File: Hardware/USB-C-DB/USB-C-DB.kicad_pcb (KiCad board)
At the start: 4 copper layers, 85.6 x 54 mm, 215 parts, among them J1 USB_C_Receptacle, J10 GND, J11 MCU_RST, J12 MCU_EN, J13 MCU_TOUT, J14 MCU_IO0, J15 EFUSE_PRG, J16 UART_DTRN, J17 UART_RTSN, J18 NOT_SUSP, J19 IBUS_S+, J2 EFPROG_POS, J20 IBUS_S-, J21 RESETN, J22 DEBUGGER, J23 +5V, J24 PWM_BC, J25 GND, J3 EFPROG_NEG, J4 BatTP+, J6 BatTP-, J7 P3V3, J8 VBUS, J9 FT_VCCIO, Q1 XP262N7002TR-G, Q10 XP262N7002TR-G, Q2 XP262N7002TR-G, Q3 XP262N7002TR-G, Q4 XP262N7002TR-G, Q5 XP262N7002TR-G, Q6 XP262N7002TR-G, Q7 XP262N7002TR-G, Q8 XP262N7002TR-G, Q9 XP262N7002TR-G, U1 NUF2221W1T2G, U10 NA555D, U2 LD1117S33TR_SOT223, U3 FT260S-U, U4 ESP-WROOM-02, U5 74HC595_mod, U6 74HC595, U7 74HC595, U8 74HC595, U9 74HC595

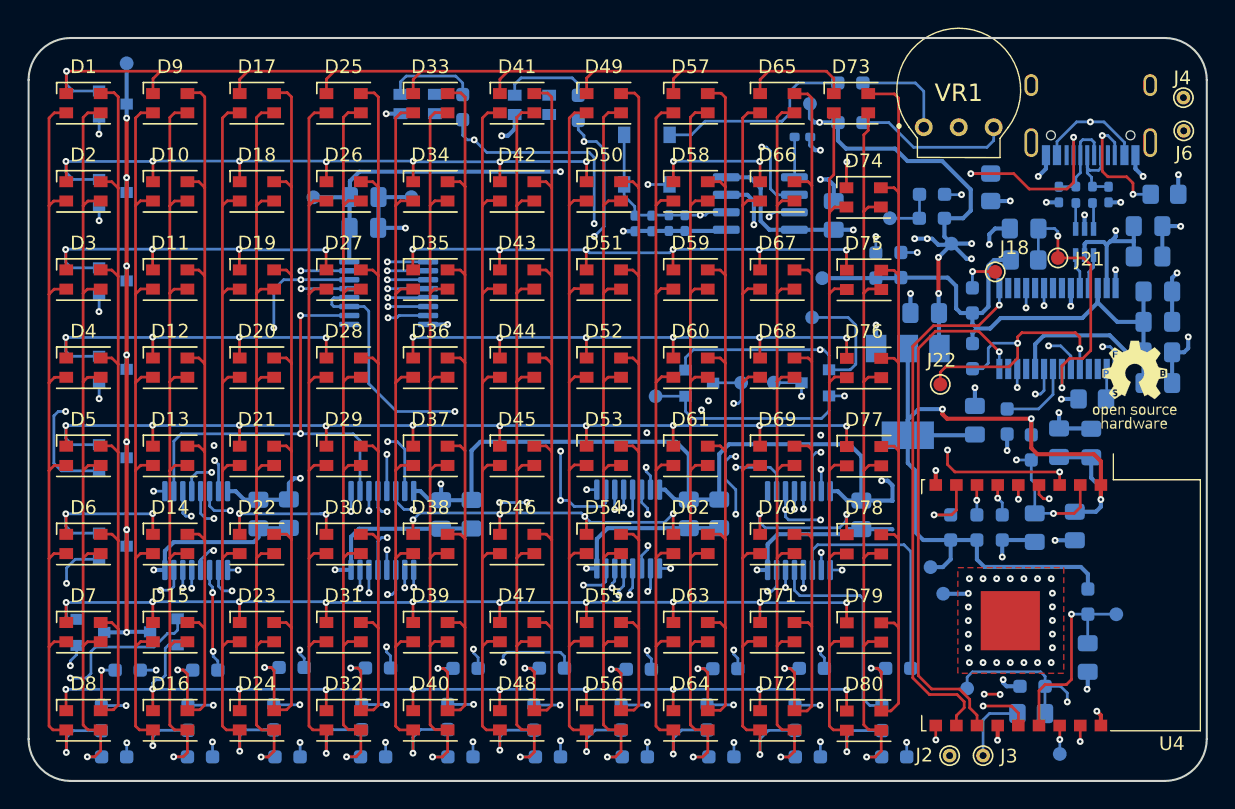
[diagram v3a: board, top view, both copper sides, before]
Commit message: Updating schematic to replace FT260 for FT231
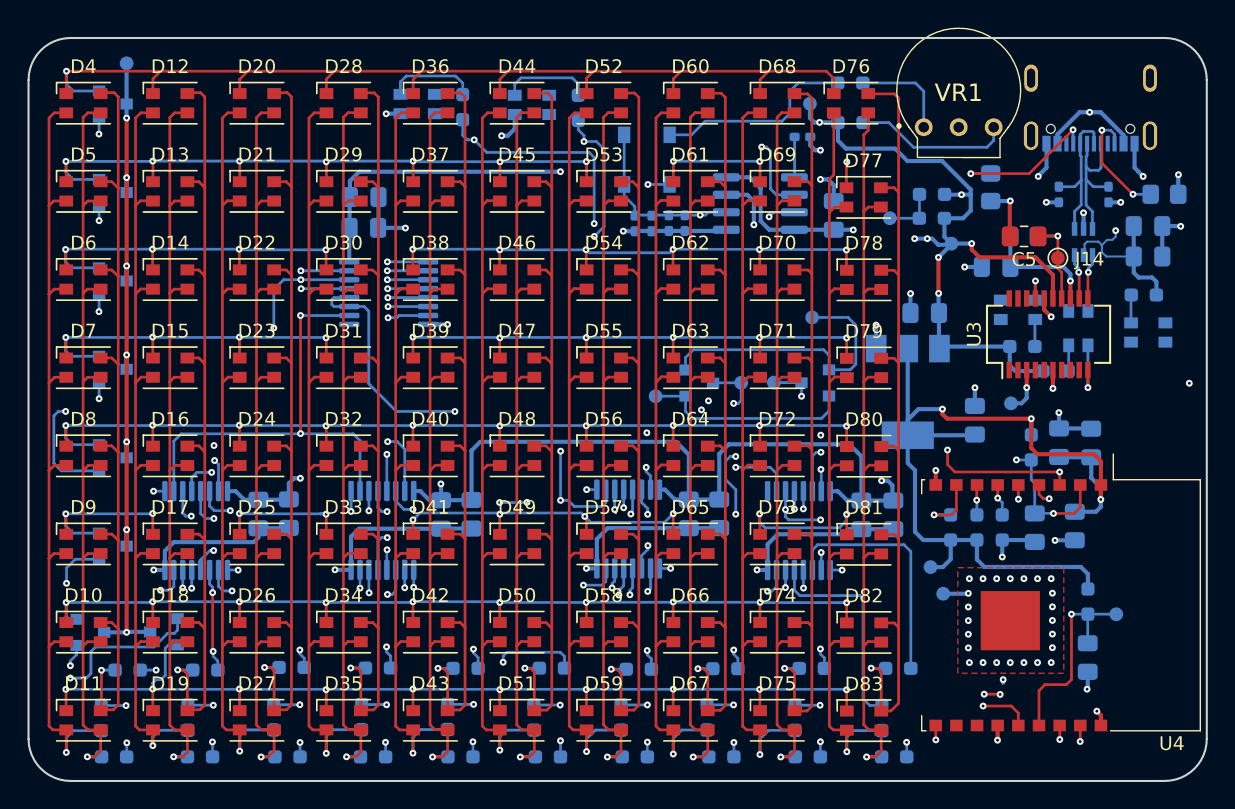
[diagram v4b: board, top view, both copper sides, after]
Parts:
- removed the C10 at (250.4, 124.4)
- removed the C2 at (240.7, 115.4)
- removed the C7 at (250.4, 122.2)
- removed the C9 at (250.4, 120.0)
- removed the J13 at (243.3, 153.6)
- removed J15: EFUSE_PRG, TestPoint:TestPoint_Pad_D1.0mm
- removed J18: NOT_SUSP, TestPoint:TestPoint_Pad_D1.0mm
- removed the J2 at (235.3, 153.7)
- removed J21: RESETN, TestPoint:TestPoint_Pad_D1.0mm
- removed J22: DEBUGGER, TestPoint:TestPoint_Pad_D1.0mm
- removed J23: +5V, TestPoint:TestPoint_Pad_D1.0mm
- removed J25: GND, TestPoint:TestPoint_Pad_D1.0mm
- removed the J3 at (237.7, 153.7)
- removed the J4 at (252.3, 105.9)
- removed the J6 at (252.3, 108.3)
- removed the R10 at (245.7, 113.0)
- removed the R11 at (230.0, 118.1)
- removed the R12 at (239.5, 129.5)
- removed the R13 at (245.7, 127.8)
- removed the R14 at (237.0, 120.7)
- removed the R6 at (237.0, 124.7)
- removed the R8 at (231.8, 118.1)
- removed the R9 at (244.5, 113.0)
- added C23: 0.1u, Capacitor_SMD:C_0805_2012Metric_Pad1.18x1.45mm_HandSolder, B.Cu at (231.2, 136.2)
- added C5: 0.1u, Capacitor_SMD:C_0805_2012Metric_Pad1.18x1.45mm_HandSolder, F.Cu at (240.7, 116.0)
- added D1: LED, LED_SMD:LED_Cree-PLCC4_3.2x2.8mm_CCW, B.Cu at (244.7, 122.7)
- added D2: LED, LED_SMD:LED_Cree-PLCC4_3.2x2.8mm_CCW, B.Cu at (240.3, 121.3)
- added D3: LED, LED_SMD:LED_Cree-PLCC4_3.2x2.8mm_CCW, B.Cu at (249.7, 123.0)
- added J14: RESETN, TestPoint:TestPoint_Pad_D1.0mm, F.Cu at (243.2, 117.6)
- added R5: 309, Resistor_SMD:R_0603_1608Metric_Pad0.98x0.95mm_HandSolder, B.Cu at (249.4, 120.3)
- G1: footprint USB-C-DB:oshw-spfb -> USB-C-DB:oshw-spfb-big; moved to B.Cu
- J1: value USB_C_Receptacle -> USB4105-GF-A; footprint Connector_USB:USB_C_Receptacle_HRO_TYPE-C-31-M-12 -> SnapEDA-imports:GCT_USB4105-GF-A
- R1: value 13k -> 309; footprint Resistor_SMD:R_0805_2012Metric_Pad1.20x1.40mm_HandSolder -> Resistor_SMD:R_0603_1608Metric_Pad0.98x0.95mm_HandSolder
- R2: value 10k -> 309
- U3: value FT260S-U -> FT231XS; footprint Mouser-imports:SOP65P640X120-28N -> Package_SO:SSOP-20_3.9x8.7mm_P0.635mm; moved to F.Cu
- moved G1 44.0 mm to (204.9, 124.5), turned to 180 degrees
- moved R1 24.9 mm to (243.0, 125.8), turned to 0 degrees
- moved R2 24.7 mm to (240.6, 124.0)
- moved J4 16.5 mm to (239.8, 128.1)
- moved C8 14.5 mm to (238.7, 118.2), turned to 180 degrees
- moved R7 1.71 mm to (240.7, 116.0)
- moved J1 1.55 mm to (245.6, 104.5)
- moved U3 0.77 mm to (242.5, 123.1)
- moved U2 0.08 mm to (245.0, 116.4)
- renumbered C4 to C1, C13 to C10, C14 to C11, C15 to C12, C16 to C13, C17 to C14, C18 to C15, C19 to C16, C20 to C17, C21 to C18, C22 to C19, C1 to C2, C23 to C20, C24 to C21, C25 to C22, C27 to C24, C28 to C25, C29 to C26, C30 to C27, C31 to C28, C32 to C29, C8 to C4, C5 to C6, C6 to C7, C11 to C8, C12 to C9, D7 to D10, D8 to D11, D9 to D12, D10 to D13, D11 to D14, D12 to D15, D13 to D16, D14 to D17, D15 to D18, D16 to D19, D17 to D20, D18 to D21, D19 to D22, D20 to D23, D21 to D24, D22 to D25, D23 to D26, D24 to D27, D25 to D28, D26 to D29, D27 to D30, D28 to D31, D29 to D32, D30 to D33, D31 to D34, D32 to D35, D33 to D36, D34 to D37, D35 to D38, D36 to D39, D1 to D4, D37 to D40, D38 to D41, D39 to D42, D40 to D43, D41 to D44, D42 to D45, D43 to D46, D44 to D47, D45 to D48, D46 to D49, D2 to D5, D47 to D50, D48 to D51, D49 to D52, D50 to D53, D51 to D54, D52 to D55, D53 to D56, D54 to D57, D55 to D58, D56 to D59, D3 to D6, D57 to D60, D58 to D61, D59 to D62, D60 to D63, D61 to D64, D62 to D65, D63 to D66, D64 to D67, D65 to D68, D66 to D69, D4 to D7, D67 to D70, D68 to D71, D69 to D72, D70 to D73, D71 to D74, D72 to D75, D73 to D76, D74 to D77, D75 to D78, D76 to D79, D5 to D8, D77 to D80, D78 to D81, D79 to D82, D80 to D83, D81 to D84, D82 to D85, D83 to D86, D84 to D87, D6 to D9, J16 to J10, J17 to J11, J19 to J12, J20 to J13, J24 to J16, J7 to J2, J8 to J3, J9 to J4, J10 to J5, J11 to J6, J12 to J7, J14 to J9, R17 to R10, R18 to R11, R19 to R12, R20 to R13, R21 to R14, R22 to R15, R23 to R16, R24 to R17, R25 to R18, R26 to R19, R27 to R20, R28 to R21, R29 to R22, R30 to R23, R31 to R24, R32 to R25, R33 to R26, R34 to R27, R35 to R28, R36 to R29, R37 to R30, R38 to R31, R39 to R32, R40 to R33, R41 to R34, R42 to R35, R43 to R36, R44 to R37, R45 to R38, R46 to R39, R47 to R40, R48 to R41, R49 to R42, R50 to R43, R51 to R44, R52 to R45, R53 to R46, R7 to R6, R5 to R7, R15 to R8, R16 to R9, U2 to U1, U1 to U2
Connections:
- FB1 pad 2: Net-(FB1-Pad2) -> +5V
- R1 pad 1: /EFUSE_PROG -> +5V
- R2 pad 1: GND -> +5V
- R2 pad 2: /EFUSE_PROG -> Net-(D2-Pad2)
- U2 pad 1: Net-(R9-Pad1) -> /USB2_N
- U2 pad 3: Net-(R10-Pad1) (its old number) -> /USB2_P
- U2 pad 4: Net-(U1-Pad4) -> /USBC_P
- U2 pad 6: Net-(U1-Pad6) -> /USBC_N
- U3 pad 1: /EFUSE_PROG -> /UART_DTRN
- U3 pad 10: /VCCIO -> /TXLED
- U3 pad 11: Net-(U3-Pad11) -> /USBC_P
- U3 pad 12: /UART_RTSN -> /USBC_N
- U3 pad 13: /UART_CTSN -> /VCCIO
- U3 pad 14: /UART_TRX_N -> /RESETN
- U3 pad 15: /UART_TRX_P -> +5V
- U3 pad 16: Net-(U3-Pad16) -> GND
- U3 pad 17: Net-(U3-Pad17) -> /RXLED
- U3 pad 18: /NOT_SUSP -> Net-(U3-Pad18)
- U3 pad 19: Net-(U3-Pad19) -> /POWER_SHDN
- U3 pad 2: Net-(R13-Pad2) (its old number) -> /UART_RTSN
- U3 pad 20: /UART_DTRN -> /UART_TRX_P
- U3 pad 3: Net-(U3-Pad3) -> /VCCIO
- U3 pad 4: Net-(U3-Pad4) -> /UART_TRX_N
- U3 pad 5: /DEBUGGER -> Net-(U3-Pad5)
- U3 pad 6: /STEST_RSTN -> GND
- U3 pad 7: /RESETN -> Net-(U3-Pad7)
- U3 pad 9: Net-(R11-Pad1) -> /UART_CTSN
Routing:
- net /UART_DTRN: track 67.9 -> 21.2 mm, vias 2 -> 0
- net /EFUSE_PROG: track 42.1 -> 0.00 mm, vias 2 -> 0
- net /UART_TRX_P: track 39.3 -> 0.01 mm, vias 1 -> 0
- net /UART_TRX_N: track 38.6 -> 0.00 mm, vias 1 -> 0
- net /VCCIO: track 54.3 -> 22.3 mm, vias 0 -> 2
- net /UART_RTSN: track 46.8 -> 15.2 mm, vias 2 -> 0
- net Net-(R11-Pad1): track 25.4 -> 0.00 mm, vias 2 -> 0
- net Net-(FB1-Pad2): track 22.9 -> 0.00 mm, vias 2 -> 0
- net /DEBUGGER: track 20.3 -> 0.00 mm, vias 2 -> 0
- net /STEST_RSTN: track 19.3 -> 0.00 mm, vias 2 -> 0
- net +5V: track 282.5 -> 268.2 mm
- net /RESETN: track 20.0 -> 7.55 mm, vias 2 -> 1
- net /NOT_SUSP: track 10.4 -> 0.00 mm, vias 2 -> 0
- net GND: track 119.9 -> 110.5 mm, vias 60 -> 58
- net Net-(U3-Pad8): track 5.62 -> 0.00 mm
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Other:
- board text added: "GitHub@Rr42 Rev: v0.7"
- board text removed: "GitHub@Rr42 Rev: v0.6.1"

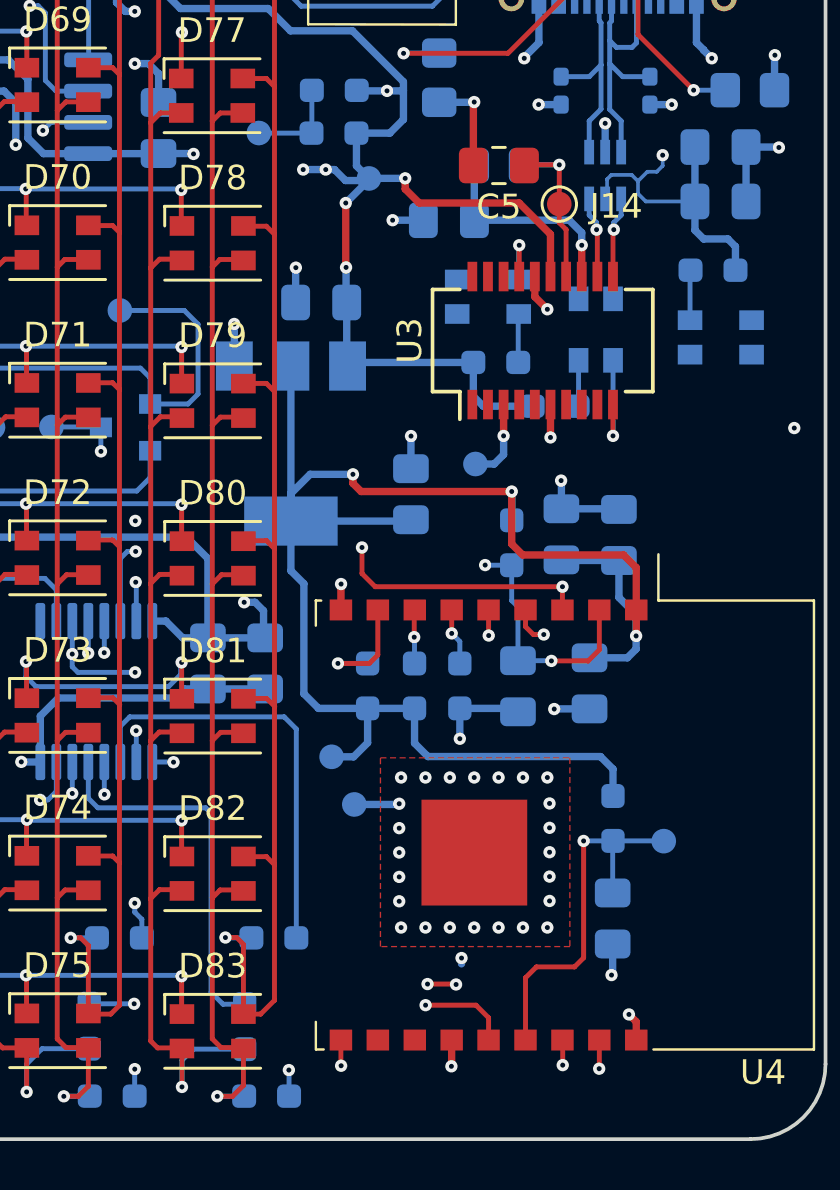
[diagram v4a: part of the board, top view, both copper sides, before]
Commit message: Updating layout to replace FT260 for FT231
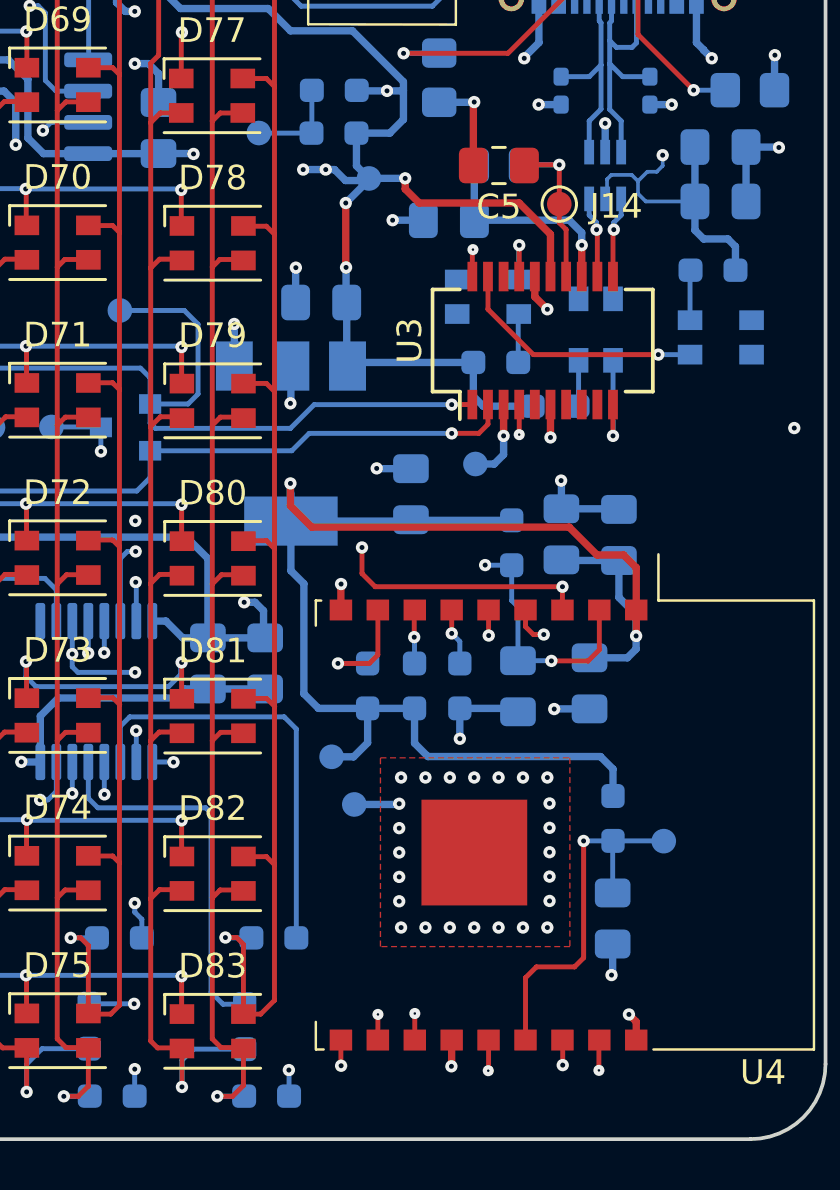
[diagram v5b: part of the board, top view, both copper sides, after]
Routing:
- net /UART_TRX_P: track 0.01 -> 45.0 mm, vias 0 -> 2
- net /UART_TRX_N: track 0.00 -> 37.6 mm, vias 0 -> 2
- net /UART_RTSN: track 15.2 -> 30.2 mm, vias 0 -> 1
- net /UART_DTRN: track 21.2 -> 35.5 mm, vias 0 -> 1
- net /POWER_SHDN: track 0.00 -> 10.3 mm, vias 0 -> 1
- net /MCU_IO5: track 113.6 -> 111.6 mm
- net +3V3: track 68.0 -> 69.6 mm
- net GND: track 110.5 -> 110.3 mm, vias 58 -> 57
- net /DCLK: vias 10 -> 8

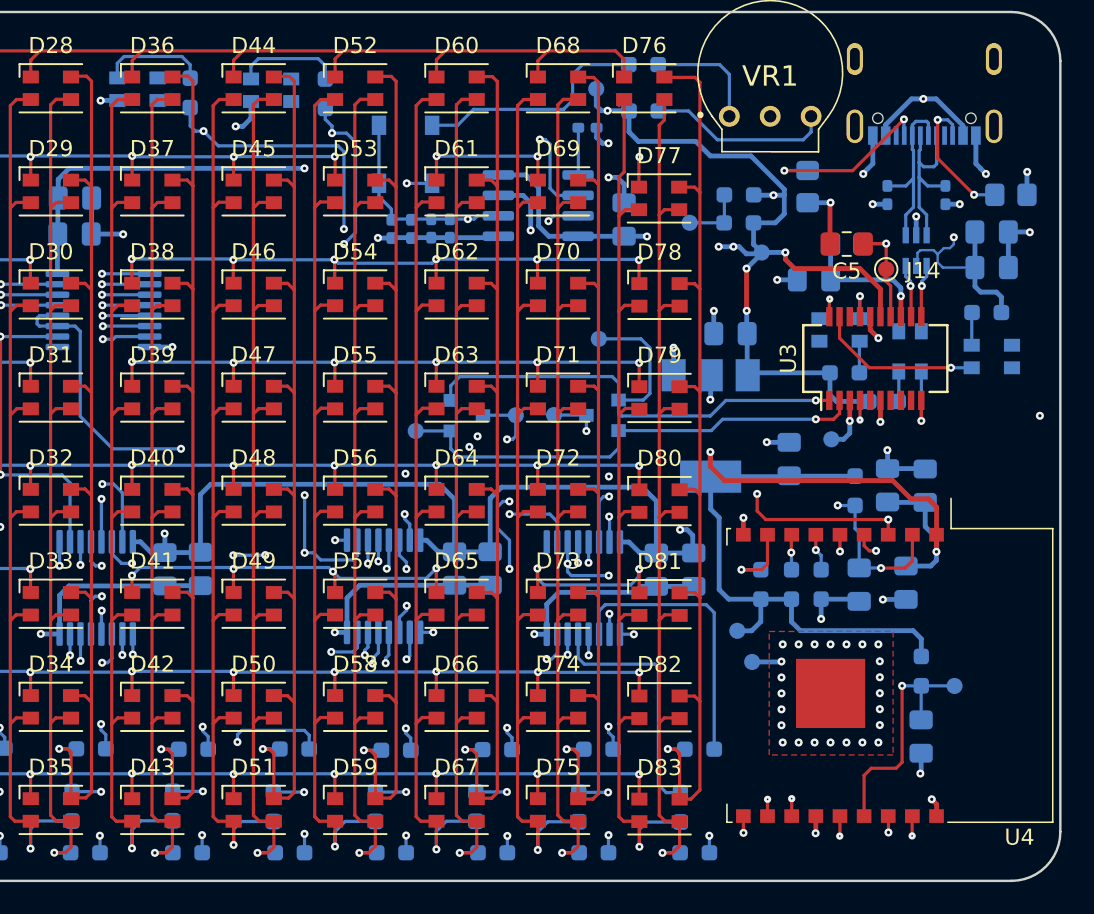
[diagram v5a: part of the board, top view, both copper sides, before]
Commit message: Fixing incorrect connection in debug LEDs
* Updating symbol to fix incorrect GND connection in debug LED
* Adding image of assembled demo
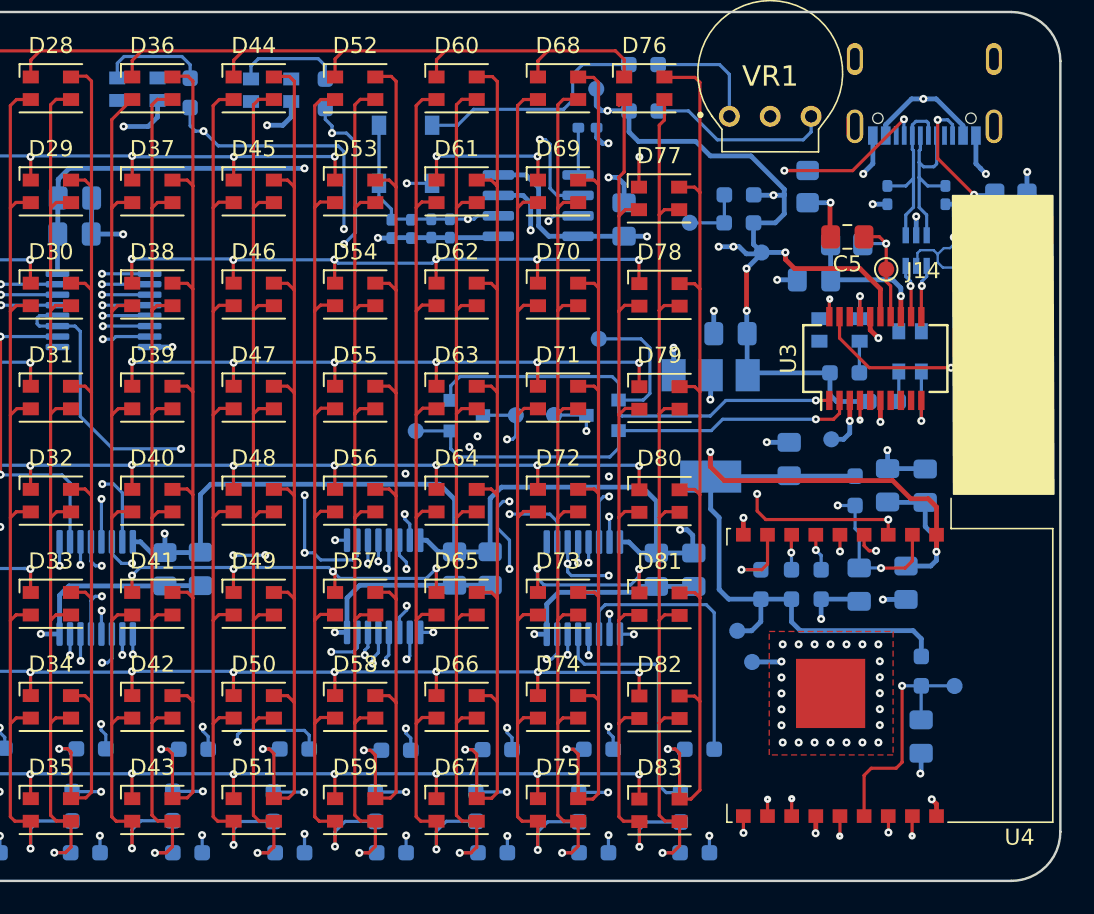
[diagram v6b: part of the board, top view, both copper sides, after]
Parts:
- added REF**: Name_pad_18x6mm, USB-C-DB:Name_pad_18x6mm, B.Cu at (189.4, 125.5)
- added REF**: Name_pad_18x6mm, USB-C-DB:Name_pad_18x6mm, B.Cu at (183.1, 125.5)
- added REF**: Name_pad_18x6mm, USB-C-DB:Name_pad_18x6mm, F.Cu at (247.4, 131.5)
- moved C5 0.45 mm to (240.8, 115.6)
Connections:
- D84 pad 1: GND -> (no net)
- D84 pad 4: (no net) -> GND
- D85 pad 1: GND -> (no net)
- D85 pad 4: (no net) -> GND
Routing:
- net GND: track 110.3 -> 113.1 mm
- net Net-(D36-Pad2): track 61.0 -> 60.5 mm
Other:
- board text added: "GitHub@Rr42 Rev: v0.7.1"
- board text removed: "GitHub@Rr42 Rev: v0.7"

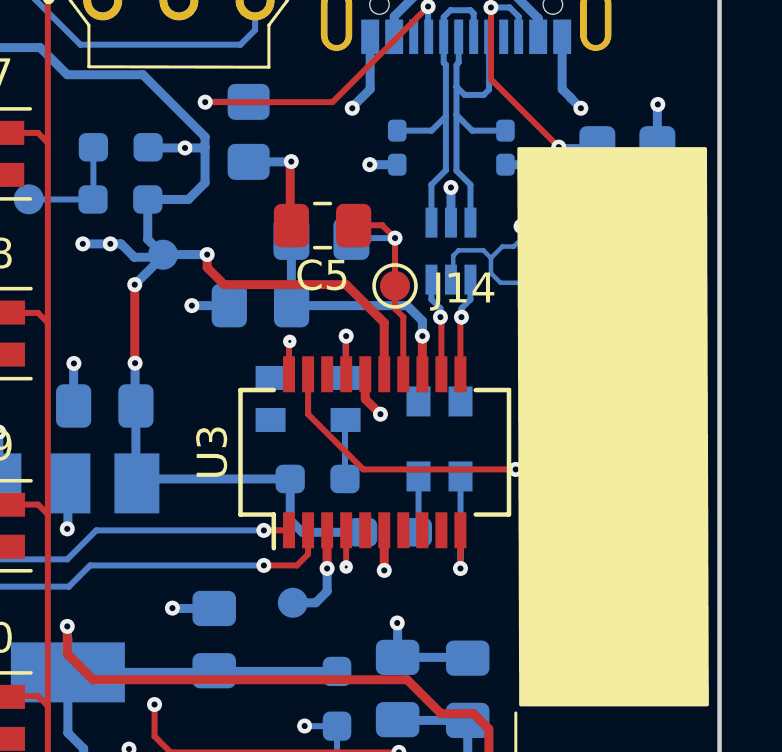
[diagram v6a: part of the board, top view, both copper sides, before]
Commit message: Patching activity LED connections and adding FTDI firmware
* Patching issue in layout where the FTDI activity LED orientations where incorrectly connected.
* Adding firmware template and instructions to modify the FT231's EEPROM firmware
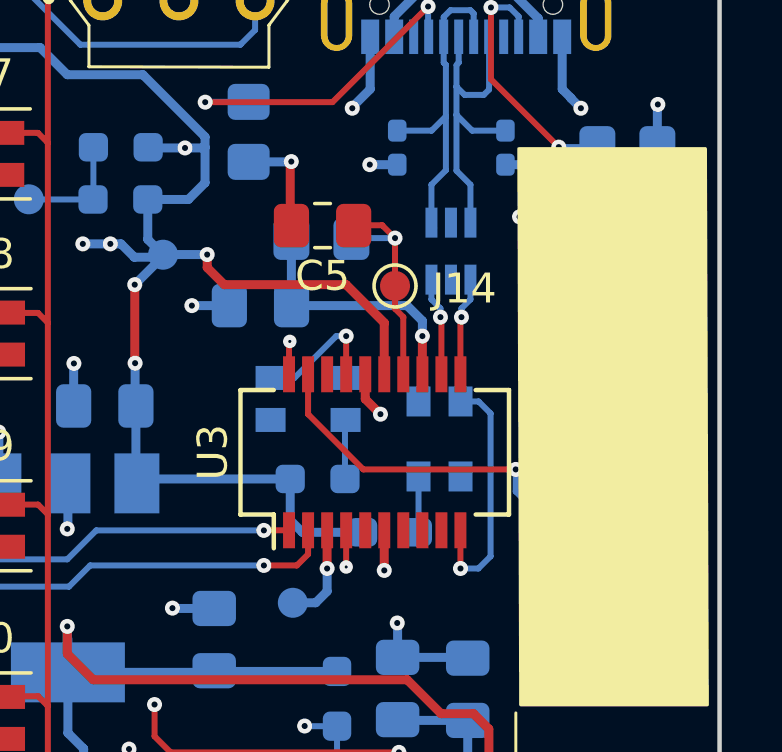
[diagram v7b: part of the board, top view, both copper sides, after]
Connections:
- D1 pad 1: /TXLED -> (no net)
- D1 pad 4: (no net) -> /TXLED
- D2 pad 1: /RXLED -> (no net)
- D2 pad 4: (no net) -> /RXLED
- D3 pad 1: /POWER_SHDN -> (no net)
- D3 pad 4: (no net) -> /POWER_SHDN
- U2 pad 2: GND -> Net-(U2-Pad2)
- U2 pad 5: +5V -> Net-(U2-Pad5)
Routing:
- net +5V: track 268.2 -> 261.7 mm
- net /POWER_SHDN: track 10.3 -> 14.6 mm
- net /TXLED: track 4.34 -> 8.38 mm
- net /RXLED: track 2.68 -> 4.40 mm
- net GND: track 113.1 -> 111.9 mm, vias 57 -> 56
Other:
- board text added: "GitHub@Rr42 Rev: v0.7.2"
- board text removed: "GitHub@Rr42 Rev: v0.7.1"

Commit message: Updating OSHW logo to include mechanicals
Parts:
- G1: footprint USB-C-DB:oshw-spfb-big -> USB-C-DB:oshw-spfmb
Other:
- board text added: "GitHub@Rr42 Rev: v0.7.3"
- board text removed: "GitHub@Rr42 Rev: v0.7.2"
